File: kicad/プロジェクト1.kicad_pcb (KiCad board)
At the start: 2 copper layers, 86.5 x 53.3 mm, 12 parts, among them J1 Barrel_Jack, Q1 2SC1815, Q2 2SA1015

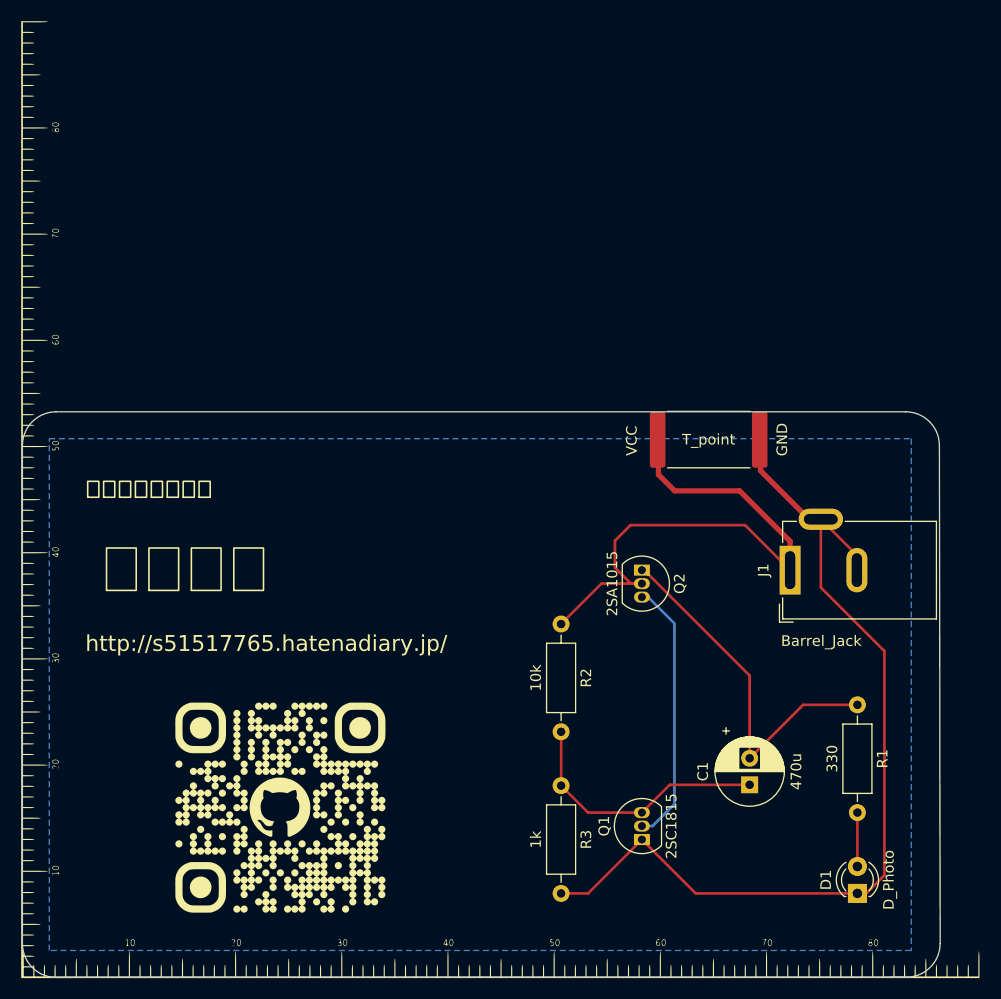
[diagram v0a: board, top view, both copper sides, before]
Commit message: 回路図を修正
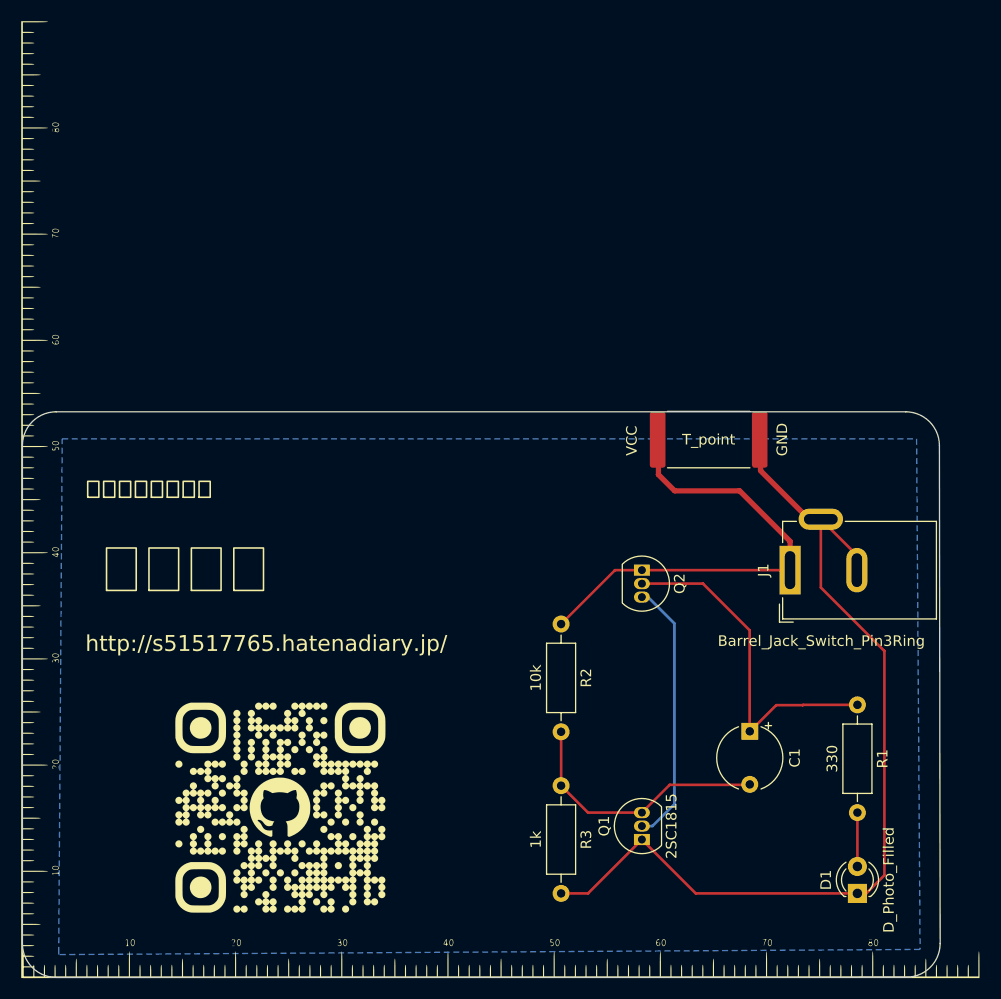
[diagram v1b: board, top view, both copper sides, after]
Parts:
- C1: value 470u -> 10u; footprint Capacitor_THT:CP_Radial_D6.3mm_P2.50mm -> Capacitor_THT:CP_Radial_Tantal_D6.0mm_P5.00mm
- D1: value D_Photo -> D_Photo_Filled
- J1: value Barrel_Jack -> Barrel_Jack_Switch_Pin3Ring
- moved C1 5.04 mm to (167.7, 103.8), turned to -90 degrees
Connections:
- C1 pad 1: Net-(Q1-B) -> Net-(Q2-C)
- C1 pad 2: Net-(Q2-E) -> Net-(Q1-B)
- J1 pad 1: Net-(Q2-C) -> Net-(Q2-E)
- R1 pad 1: Net-(Q2-E) -> Net-(Q2-C)
- R2 pad 1: Net-(Q2-C) -> Net-(Q2-E)
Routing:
- net Net-(Q2-E): track 34.3 -> 23.1 mm
- net Net-(Q2-C): track 53.1 -> 52.1 mm
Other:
- board text added: "Rev.2"
